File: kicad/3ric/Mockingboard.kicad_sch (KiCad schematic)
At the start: 17 parts, among them CON1 SJ-3523-SMT-TR, T1_VIA1 65C22S, T2_VIA1 65C22S

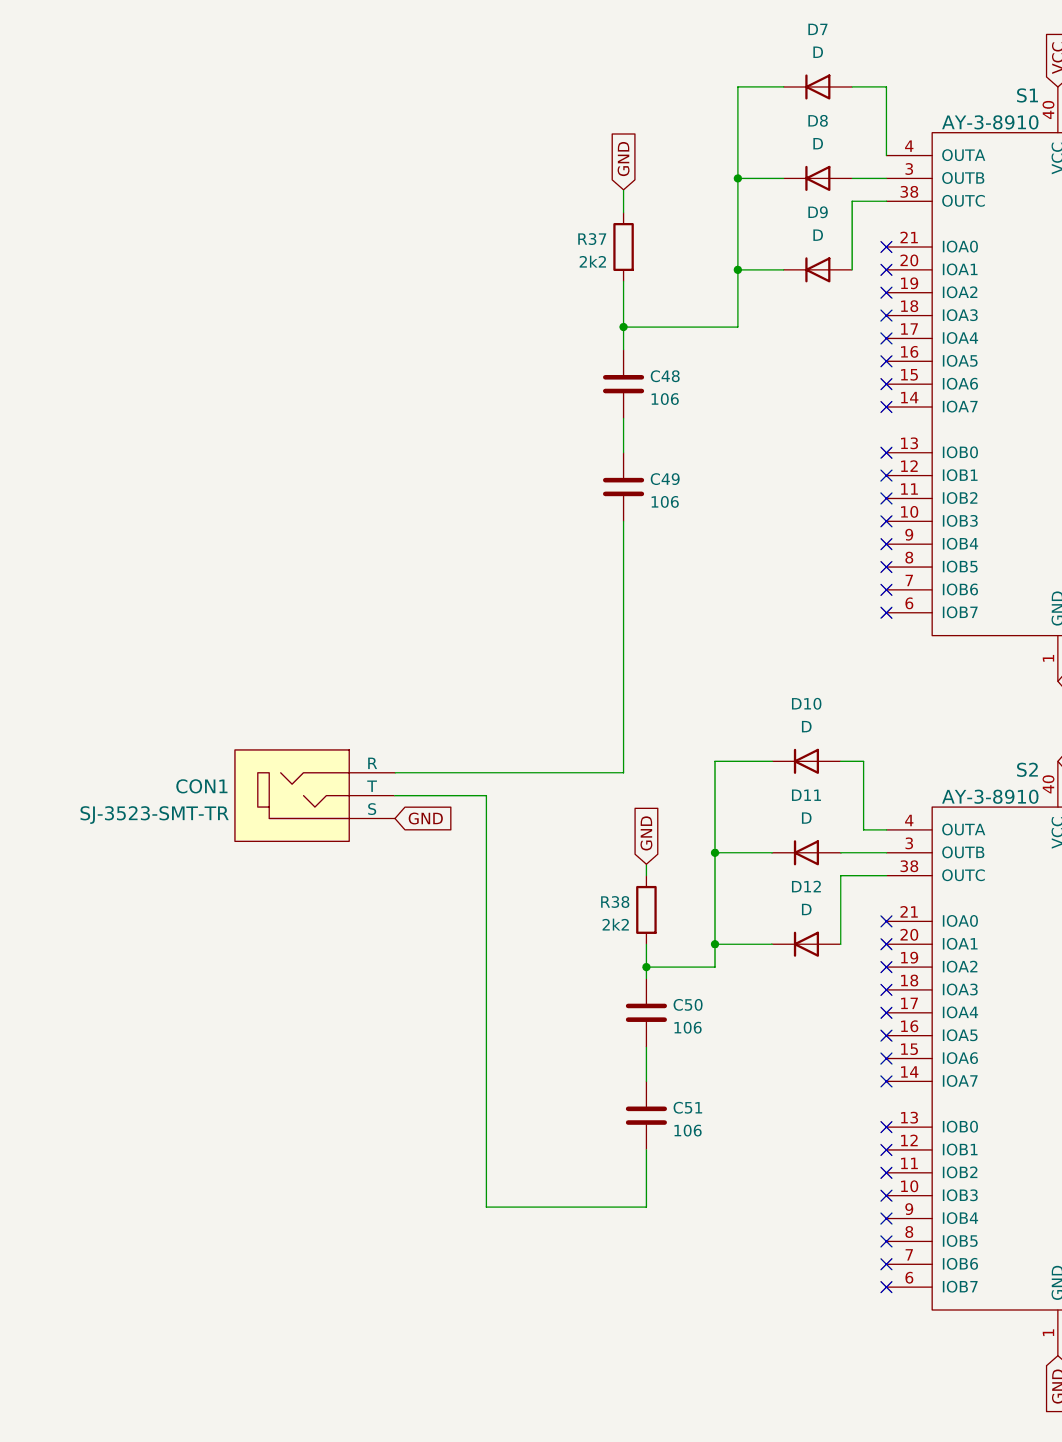
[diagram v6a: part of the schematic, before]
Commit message: updated schematics and PCB PNG of the breadboard layout
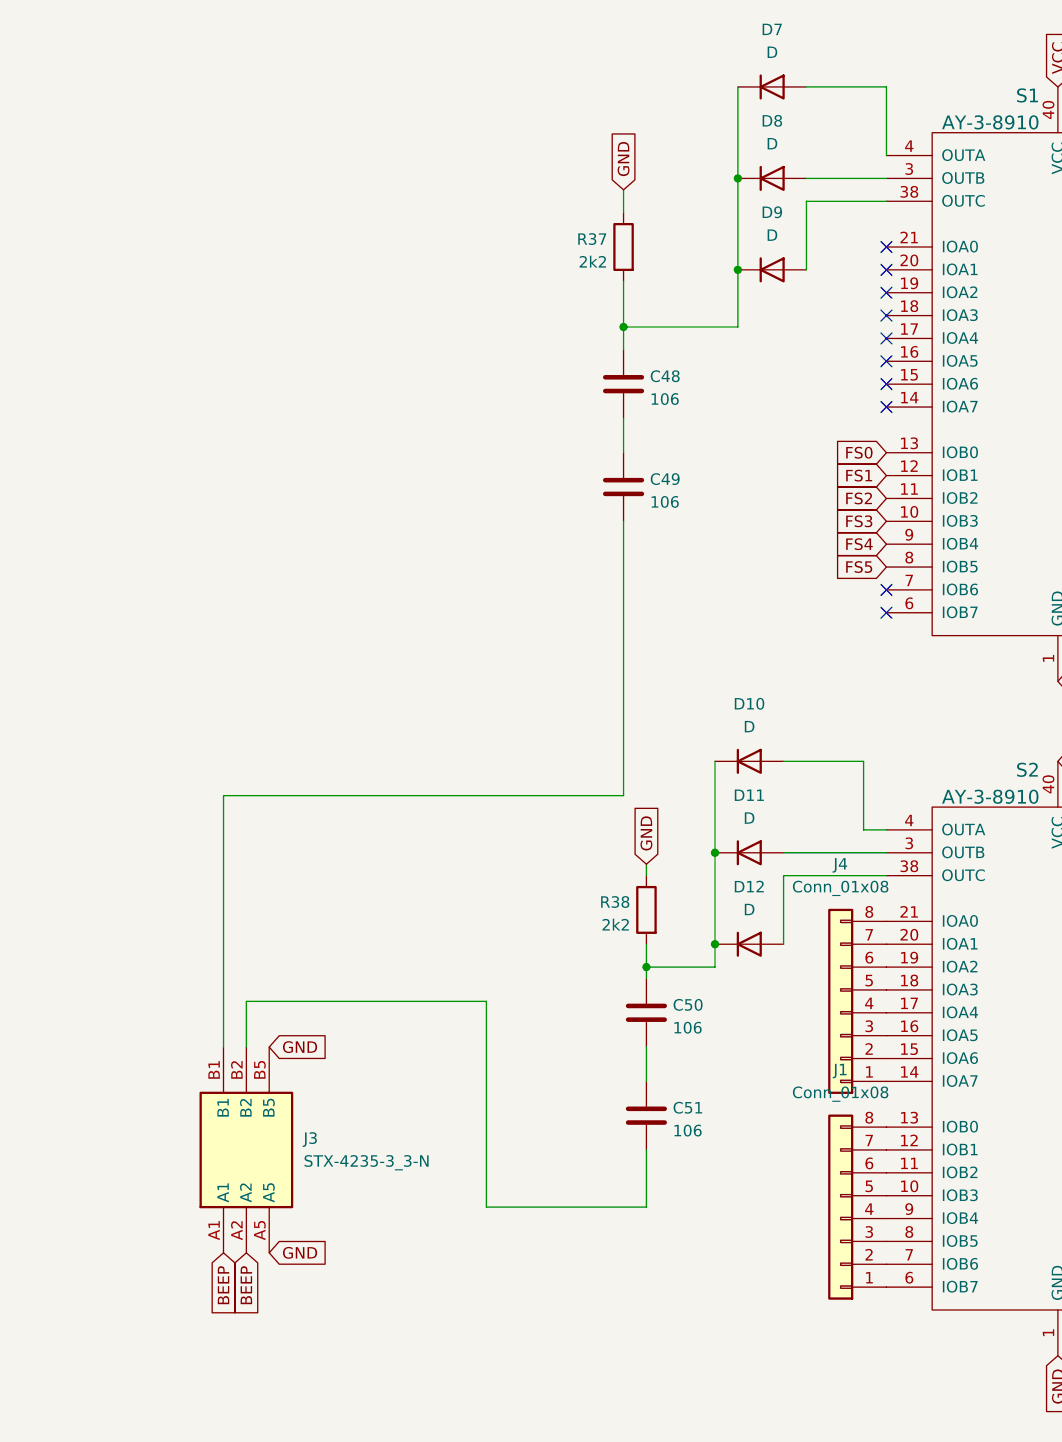
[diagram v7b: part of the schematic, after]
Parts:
- removed CON1: SJ-3523-SMT-TR, digikey-footprints:Switch_Slide_11.6x4mm_SJ-3523-SMT, symbol dk_Barrel-Audio-Connectors:SJ-3523-SMT-TR
- added J1, J4: Conn_01x08, Connector_PinHeader_2.54mm:PinHeader_1x08_P2.54mm_Vertical, symbol Connector_Generic:Conn_01x08
- added J3: STX-4235-3_3-N, audiojack:STX423533N, symbol STX-4235-3_3-N:STX-4235-3_3-N
- C48, C49, C50, C51: footprint Capacitor_THT:C_Axial_L3.8mm_D2.6mm_P7.50mm_Horizontal -> Capacitor_SMD:C_0603_1608Metric_Pad1.08x0.95mm_HandSolder
- D10, D11, D12, D7, D8, D9: footprint Diode_THT:D_A-405_P10.16mm_Horizontal -> Diode_SMD:D_SMA-SMB_Universal_Handsoldering
- R37, R38: footprint Resistor_THT:R_Axial_DIN0207_L6.3mm_D2.5mm_P7.62mm_Horizontal -> Resistor_SMD:R_0805_2012Metric_Pad1.20x1.40mm_HandSolder
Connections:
- net GND: now also J3.A5, J3.B5
- net at S2.10 (IOB3): now also J1.5 (Pin_5)
- net at S2.11 (IOB2): now also J1.6 (Pin_6)
- net at S2.12 (IOB1): now also J1.7 (Pin_7)
- net at S2.13 (IOB0): now also J1.8 (Pin_8)
- net at S2.14 (IOA7): now also J4.1 (Pin_1)
- net at S2.15 (IOA6): now also J4.2 (Pin_2)
- net at S2.16 (IOA5): now also J4.3 (Pin_3)
- net at S2.17 (IOA4): now also J4.4 (Pin_4)
- net at S2.18 (IOA3): now also J4.5 (Pin_5)
- net at S2.19 (IOA2): now also J4.6 (Pin_6)
- net at S2.20 (IOA1): now also J4.7 (Pin_7)
- net at S2.21 (IOA0): now also J4.8 (Pin_8)
- net at S2.6 (IOB7): now also J1.1 (Pin_1)
- net at S2.7 (IOB6): now also J1.2 (Pin_2)
- net at S2.8 (IOB5): now also J1.3 (Pin_3)
- net at S2.9 (IOB4): now also J1.4 (Pin_4)
- net at C49.2: now also J3.B1
- net FS3: now reaches S1.10 (IOB3)
- net FS2: now reaches S1.11 (IOB2)
- net FS1: now reaches S1.12 (IOB1)
- net FS0: now reaches S1.13 (IOB0)
- net FS5: now reaches S1.8 (IOB5)
- net FS4: now reaches S1.9 (IOB4)
- net at C51.2: now also J3.B2
- new net BEEP: J3.A1, J3.A2
- no-connect marks 58 -> 36
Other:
- moved on the sheet: D10, D11, D12, D7, D8, D9

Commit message: pcb layout continued
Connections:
- net BEEP: now also J3.A5; no longer J3.A1
- net GND: now also J3.A1, J3.B1; no longer J3.A5, J3.B5
- net at C49.2: now also J3.B5; no longer J3.B1
